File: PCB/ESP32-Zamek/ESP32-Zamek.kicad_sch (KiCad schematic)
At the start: 12 parts, among them J1 USB_C_Receptacle_USB2.0_16P, Q1 2SC4213, Q2 2SC4213, U1 ESP32-WROOM-32D, U2 FT232RNL-REEL

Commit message: Poczatki NFC
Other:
- added sheet nfc (nfc.kicad_sch)
- company: (none) -> Onyks - Warsaw University of Technology
- title: (none) -> Onyks IoT Control Cabinet

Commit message: NFC - znaleziono dokumentację projektową xD
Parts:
- removed Q1, Q2: 2SC4213, Package_TO_SOT_SMD:SOT-323_SC-70, symbol Transistor_BJT:2SC4213
- removed R3, R4: 10k, symbol Device:R
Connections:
- no-connect marks 19 -> 20

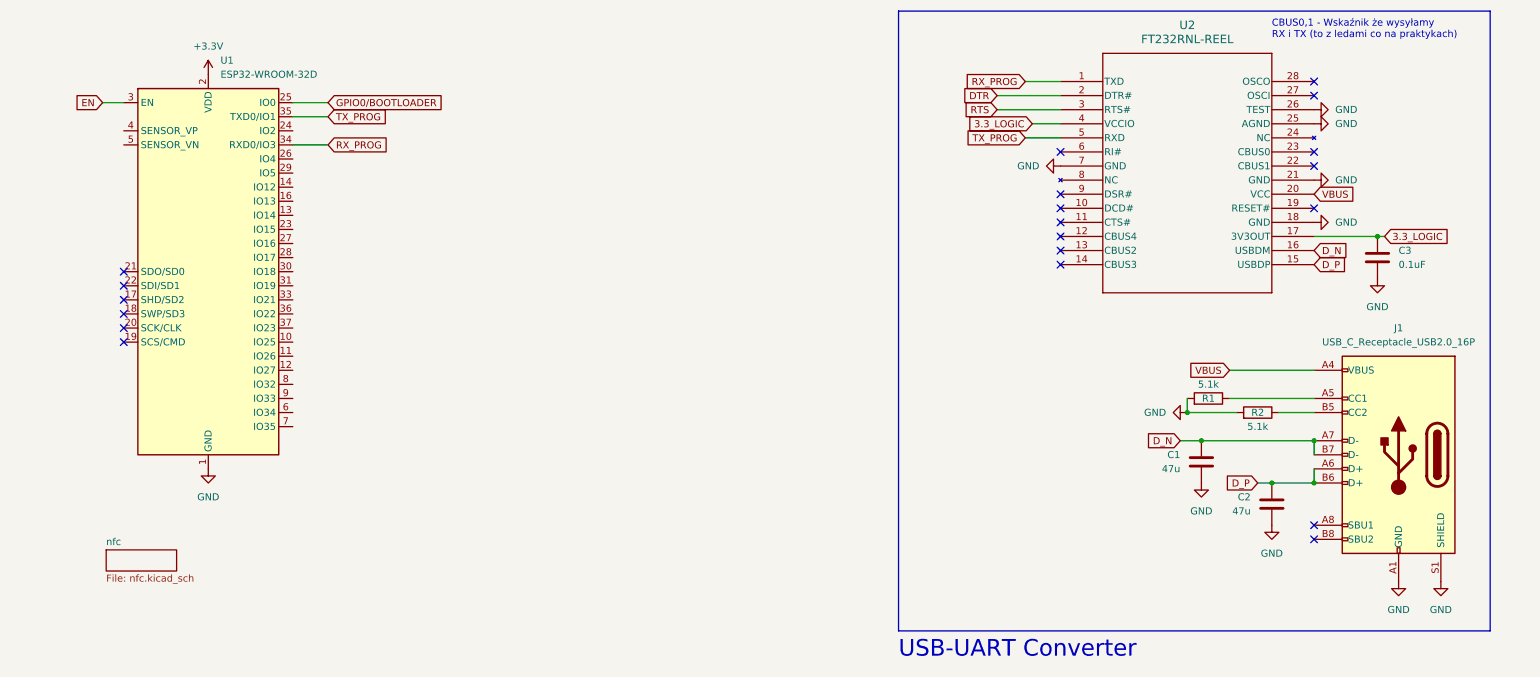
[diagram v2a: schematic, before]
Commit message: Booting/Reset circuit change
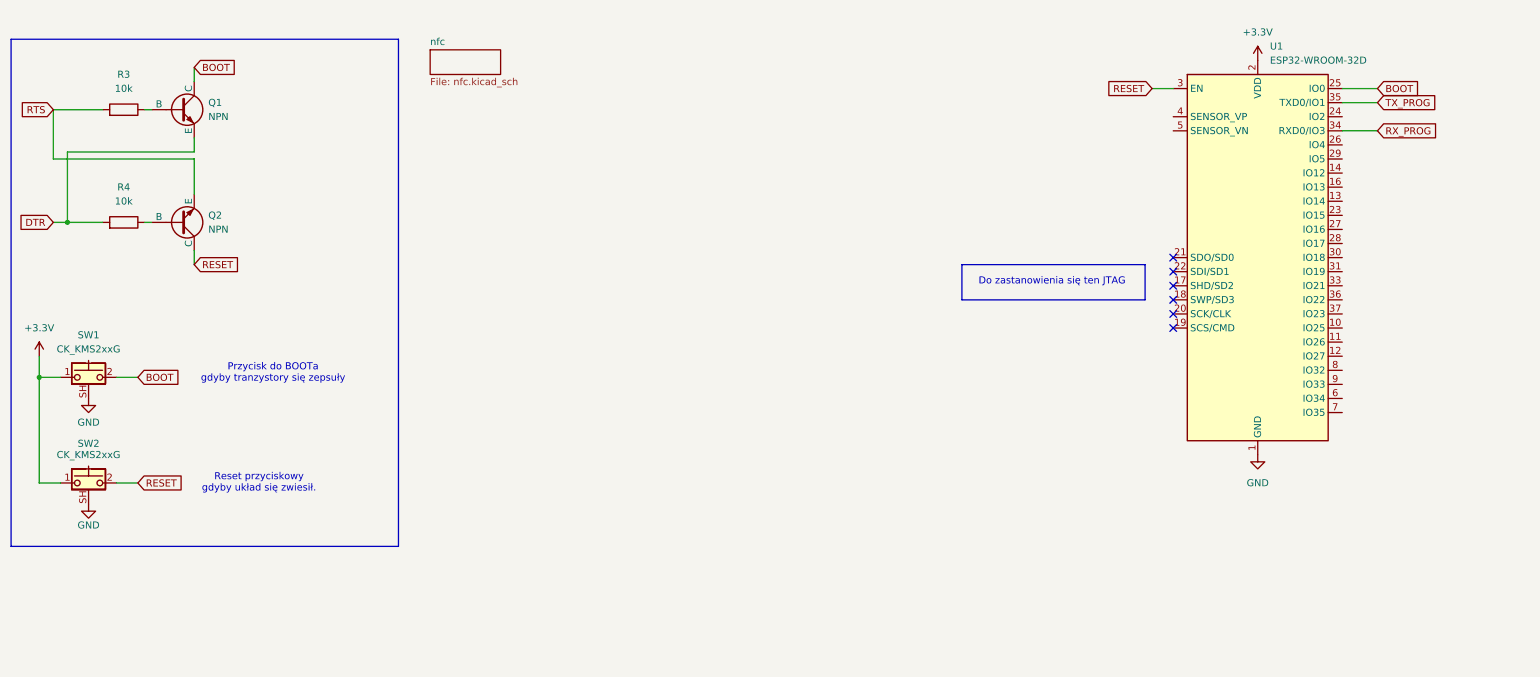
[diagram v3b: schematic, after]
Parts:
- removed C1, C2: 47u, symbol Device:C
- removed C3: 0.1uF, symbol Device:C
- removed J1: USB_C_Receptacle_USB2.0_16P, Connector_USB:USB_C_Receptacle_GCT_USB4085, symbol Connector:USB_C_Receptacle_USB2.0_16P
- removed R1, R2: 5.1k, symbol Device:R
- removed U2: FT232RNL-REEL, SSOP-28_FTD, symbol 2024-11-08_21-05-18:FT232RNL-REEL
- added Q1, Q2: NPN, symbol Simulation_SPICE:NPN
- added R3, R4: 10k, symbol Device:R
- added SW1, SW2: CK_KMS2xxG, Button_Switch_SMD:SW_SPST_CK_KMS2xxGP, symbol Switch:CK_KMS2xxG
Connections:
- net +3.3V: now also SW1.1, SW2.1
- net DTR: now also Q1.3 (E), R4.2
- net GND: now also SW1.SH (B), SW2.SH (B)
- net RTS: now also Q2.3 (E), R3.2
- net EN renamed RESET
- net RESET: now also Q2.1 (C), SW2.2
- net GPIO0/BOOTLOADER renamed BOOT
- net BOOT: now also Q1.1 (C), SW1.2
- new net: Q2.2 (B), R4.1
- new net: Q1.2 (B), R3.1
- no-connect marks 20 -> 6
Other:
- note added: "Do zastanowienia się ten JTAG"
- note added: "Przycisk do BOOTa gdyby tranzystory się zepsuły"
- note added: "Reset przyciskowy gdyby układ się zwiesił."
- note removed: "CBUS0,1 - Wskaźnik że wysyłamy RX i TX (to z ledami co na praktykach)"
- note removed: "USB-UART Converter"
- moved on the sheet: U1

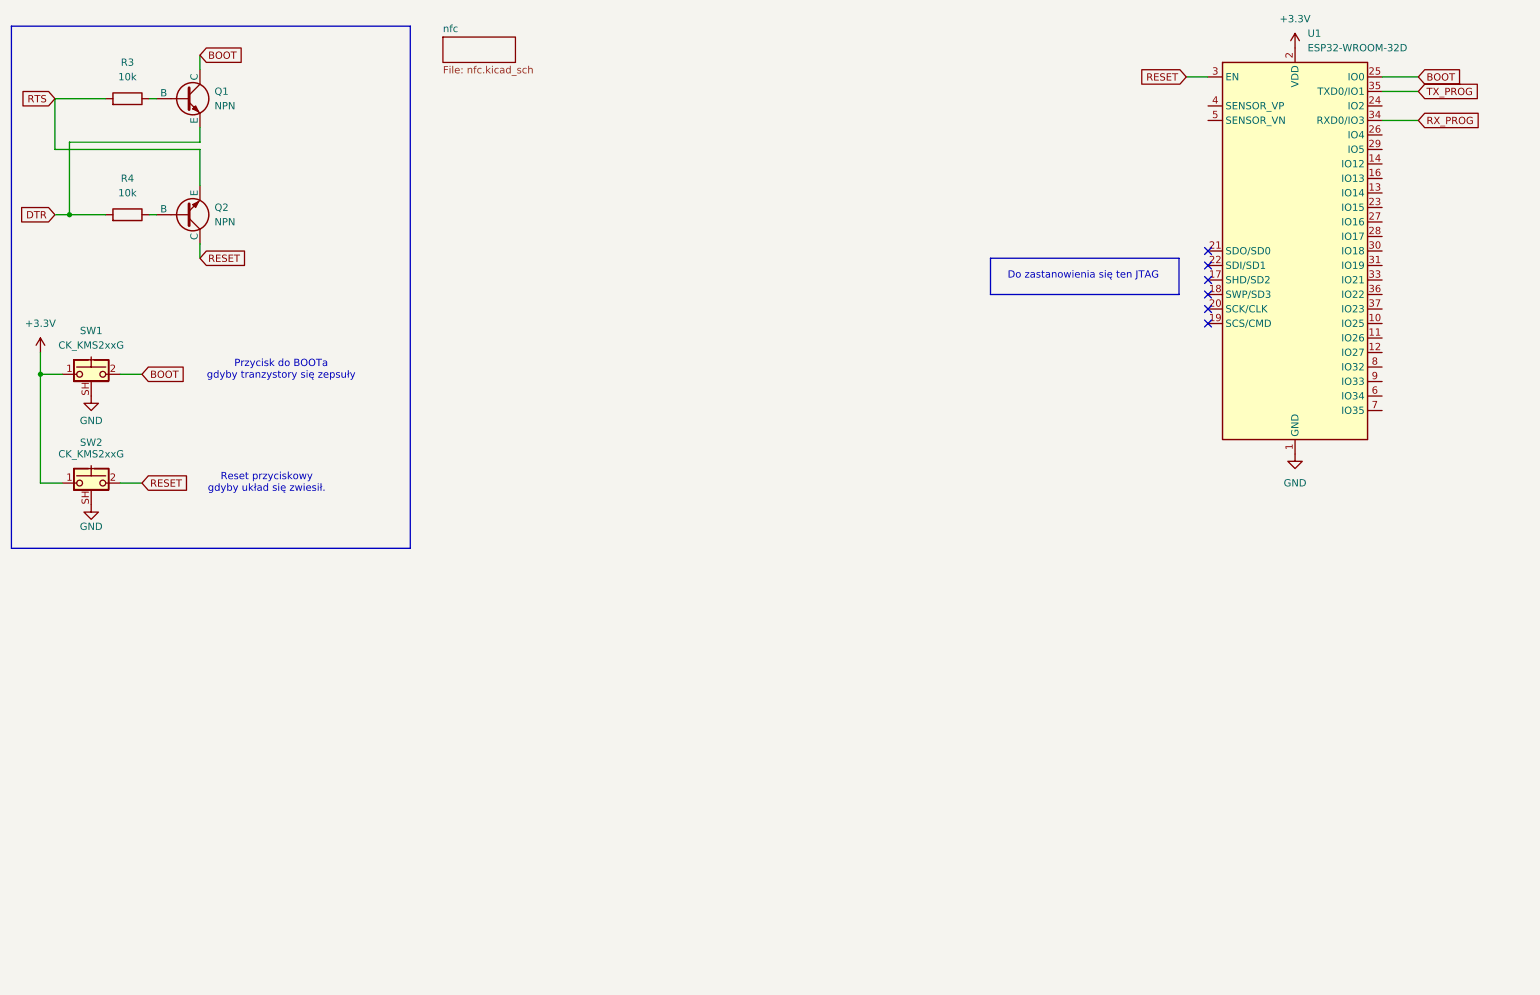
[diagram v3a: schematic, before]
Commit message: Small changes to the buttons and lock control
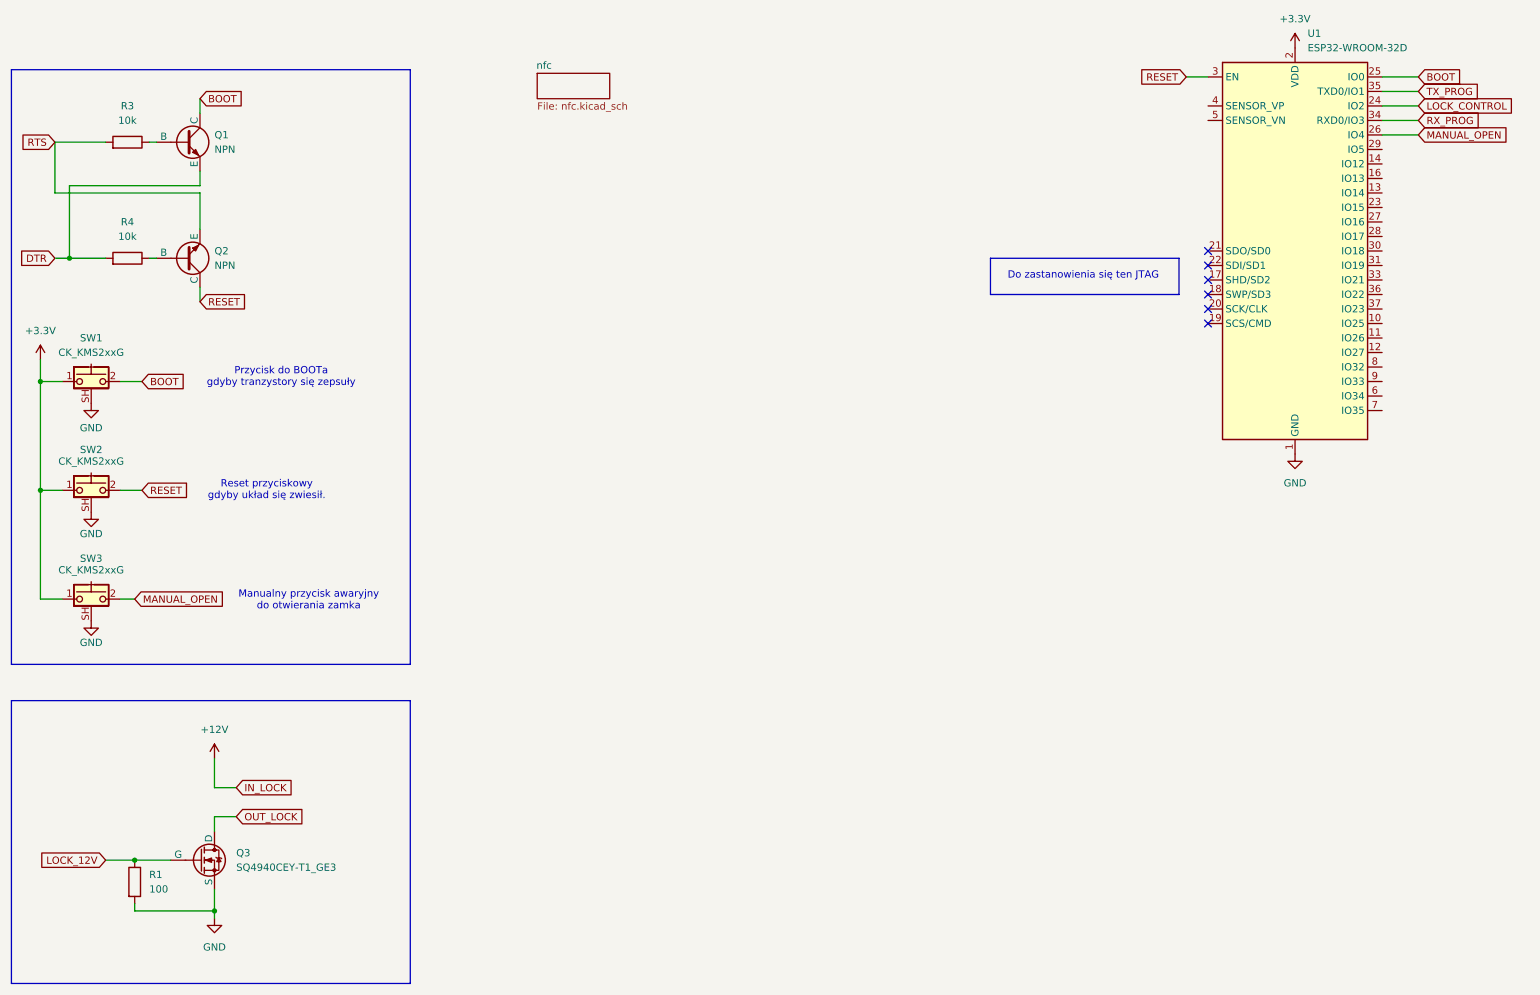
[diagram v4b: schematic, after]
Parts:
- added Q3: SQ4940CEY-T1_GE3, symbol Simulation_SPICE:NMOS
- added R1: 100, symbol Device:R
- added SW3: CK_KMS2xxG, Button_Switch_SMD:SW_SPST_CK_KMS2xxGP, symbol Switch:CK_KMS2xxG
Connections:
- net +3.3V: now also SW3.1
- net GND: now also Q3.3 (S), R1.2, SW3.SH (B)
- net LOCK_CONTROL: now reaches U1.24 (IO2)
- net MANUAL_OPEN: now reaches U1.26 (IO4)
- net MANUAL_OPEN: now also SW3.2
- new net LOCK_12V: Q3.2 (G), R1.1
- new net OUT_LOCK: Q3.1 (D)
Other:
- note added: "Manualny przycisk awaryjny do otwierania zamka"
- moved on the sheet: Q1, Q2, R3, R4, SW1, SW2

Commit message: Add the nfc connector with external outputs
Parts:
- added J? (x2): Conn_01x02, symbol Connector_Generic:Conn_01x02
- added J?: Conn_01x08_Socket, symbol Connector:Conn_01x08_Socket
- added J? (x2): Conn_01x02_Socket, symbol Connector:Conn_01x02_Socket
- added R? (x2): 10k, symbol Device:R
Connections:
- net LOCK_CONTROL is gone; now on net LOCK_MCU_ON_OFF: U1.24 (IO2)
- net +12V: now also J?.1 (Pin_1), J?.1 (Pin_1)
- net +3.3V: now also J?.1 (Pin_1), J?.1 (Pin_1), J?.8 (Pin_8), R?.1, R?.1
- net GND: now also J?.6 (Pin_6)
- net MANUAL_OPEN: no longer SW3.2
- net LOCK_12V renamed LOCK_MCU_ON_OFF
- net OUT_LOCK renamed LOCK_MINUS
- net LOCK_MINUS: now also J?.2 (Pin_2), J?.2 (Pin_2)
- new net LOCK_MCU_MANUAL_OPEN: J?.2 (Pin_2), J?.2 (Pin_2), SW3.2
- new net NFC_IRQ: J?.5 (Pin_5)
- new net NFC_MISO: J?.4 (Pin_4)
- new net NFC_MOSI: J?.3 (Pin_3)
- new net NFC_RST: J?.7 (Pin_7)
- new net NFC_SCK: J?.2 (Pin_2), R?.2
- new net NFC_SDA: J?.1 (Pin_1), R?.2
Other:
- removed sheet nfc
- note added: "ESP32 MCU"
- note added: "ESP32 MCU Programmer"
- note added: "Lock Connector"
- note added: "Lock Controller"
- note added: "Lock Manually Opener"
- note added: "NFC Connector"
- note removed: "Manualny przycisk awaryjny do otwierania zamka"
- note removed: "Przycisk do BOOTa gdyby tranzystory się zepsuły"
- note removed: "Reset przyciskowy gdyby układ się zwiesił."
- moved on the sheet: Q1, Q2, Q3, R1, R3, R4, SW1, SW2, SW3, U1

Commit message: Updates of the schematics and add the README.md; add a step-down for 3V3
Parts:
- removed J? (x2): Conn_01x02, symbol Connector_Generic:Conn_01x02
- removed J?: Conn_01x08_Socket, symbol Connector:Conn_01x08_Socket
- removed Q1, Q2: NPN, symbol Simulation_SPICE:NPN
- removed R3, R4, R? (x2): 10k, symbol Device:R
- removed SW1, SW2: CK_KMS2xxG, Button_Switch_SMD:SW_SPST_CK_KMS2xxGP, symbol Switch:CK_KMS2xxG
- removed U1: ESP32-WROOM-32D, RF_Module:ESP32-WROOM-32D, symbol RF_Module:ESP32-WROOM-32D
- added J? (x2): Screw_Terminal_01x02, symbol Connector:Screw_Terminal_01x02
- added Q? (x2): NPN, symbol Simulation_SPICE:NPN
- added R? (x2): 10k, symbol Device:R
- added SW? (x2): CK_KMS2xxG, Button_Switch_SMD:SW_SPST_CK_KMS2xxGP, symbol Switch:CK_KMS2xxG
- added U?: ESP32-WROOM-32D, RF_Module:ESP32-WROOM-32D, symbol RF_Module:ESP32-WROOM-32D
- gave numbers to parts that had none: 2
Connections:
- net +12V: now also J?.1 (Pin_1)
- net +3.3V: now also J?.1 (Pin_1), SW?.1, SW?.1, U?.2 (VDD)
- net DTR: now also Q?.3 (E), R?.2
- net GND: now also SW?.SH (B), SW?.SH (B), U?.1 (GND), U?.15 (GND), U?.38 (GND), U?.39 (GND)
- net LOCK_MCU_MANUAL_OPEN: now also J?.2 (Pin_2), U?.31 (IO19)
- net LOCK_MINUS: now also J?.2 (Pin_2)
- net NFC_IRQ: now also U?.11 (IO26)
- net NFC_MISO: now also U?.10 (IO25)
- net NFC_MOSI: now also U?.37 (IO23)
- net NFC_RST: now also U?.12 (IO27)
- net RTS: now also Q?.3 (E), R?.2
- net LOCK_MCU_ON_OFF renamed LOCK_SWITCH
- net LOCK_SWITCH: now also U?.30 (IO18)
- new net: Q?.2 (B), R?.1 (x2)
- new net BUZZER_SWITCH: U?.26 (IO4)
- new net JTAG_MTCK: U?.16 (IO13)
- new net JTAG_MTDI: U?.14 (IO12)
- new net JTAG_MTDO: U?.23 (IO15)
- new net JTAG_MTMS: U?.13 (IO14)
- new net MCU_BOOT: Q?.1 (C), SW?.2, U?.25 (IO0)
- new net MCU_RESET: Q?.1 (C), SW?.2, U?.3 (EN)
- new net MCU_RX_PROG: U?.34 (RXD0/IO3)
- new net MCU_TX_PROG: U?.35 (TXD0/IO1)
- new net NFC_EEPROM_SCL: U?.36 (IO22)
- new net NFC_EEPROM_SDA: U?.33 (IO21)
- new net RGB_PWM_B: U?.9 (IO33)
- new net RGB_PWM_G: U?.6 (IO34)
- new net RGB_PWM_R: U?.8 (IO32)
- no-connect marks 6 -> 12
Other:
- added sheet Power Supply and NFC Connector (power_supply.kicad_sch)
- note added: "EEPROM"
- note added: "JTAG"
- note added: "NIE WIEM CO TO"
- note added: "RGB LED"
- note removed: "NFC Connector"
- company: Onyks - Warsaw University of Technology -> ,,Onyks'' Students Scientific Association
- moved on the sheet: J1, J4, Q3, R1, SW3
